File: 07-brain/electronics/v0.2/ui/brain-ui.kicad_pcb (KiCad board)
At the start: 2 copper layers, 58 x 110 mm, 55 parts, among them J1 Conn_02x03_Odd_Even, J2 Conn_01x02, J3 Conn_01x02, J4 Conn_02x02_Odd_Even, J5 Conn_02x03_Odd_Even, J6 Conn_02x02_Odd_Even, J7 Conn_02x05_Odd_Even, J8 Conn_02x03_Odd_Even, Q1 2N3904, Q2 2N3904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

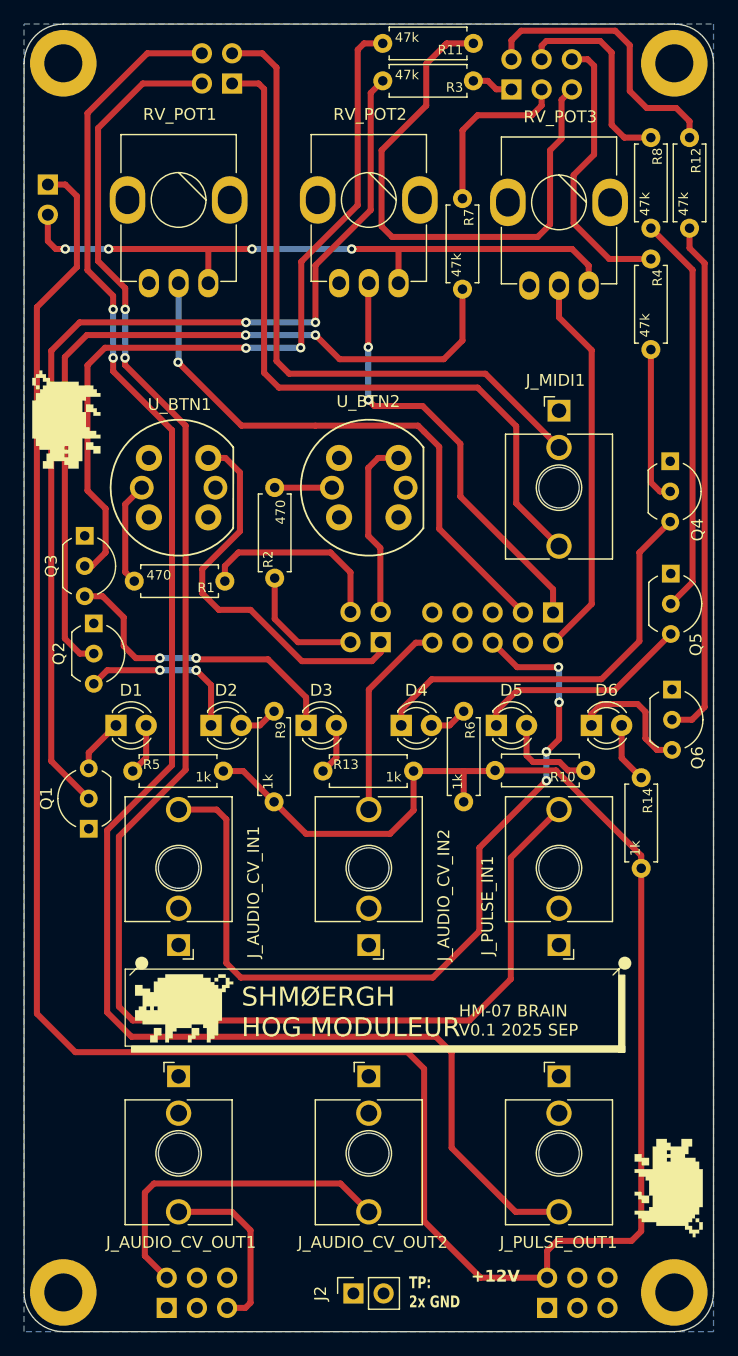
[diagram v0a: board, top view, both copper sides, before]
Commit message: Removed one pot and added one button in Brain
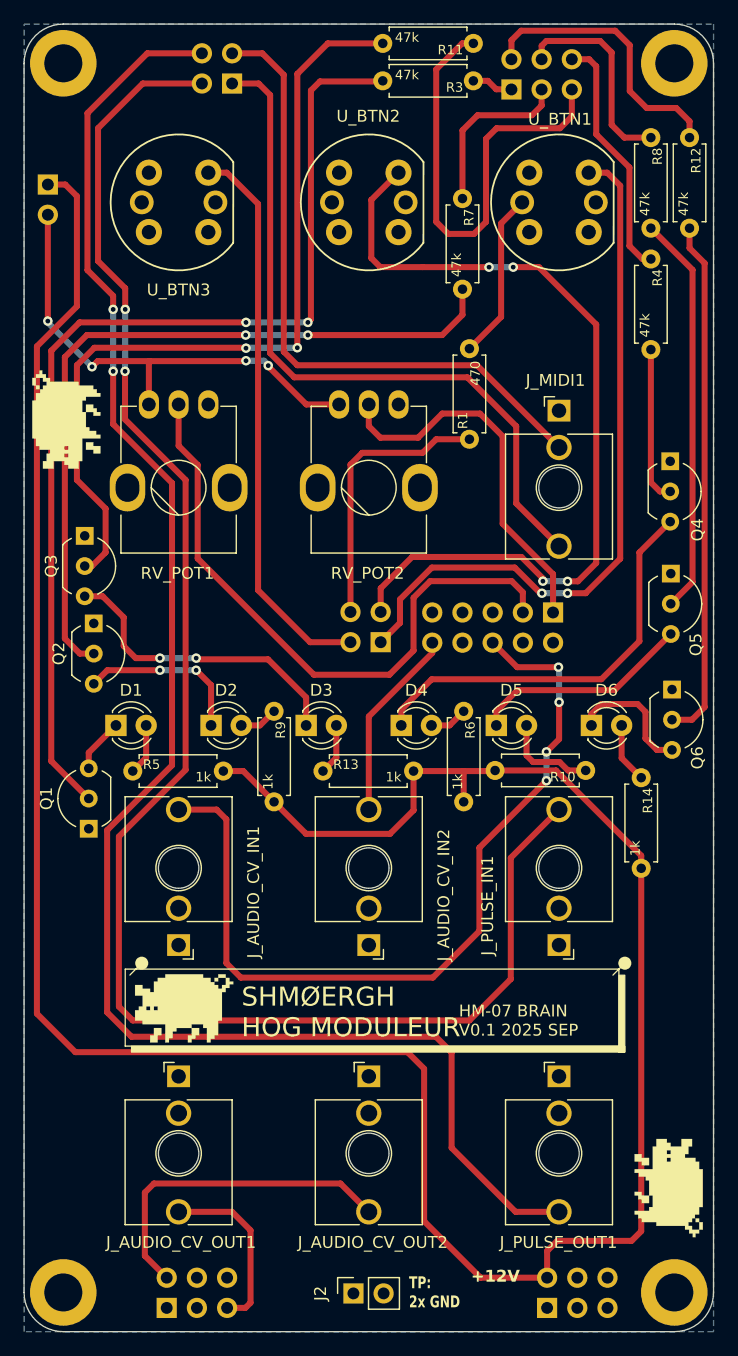
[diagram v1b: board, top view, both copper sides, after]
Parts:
- removed R2: 470, Shmoergh_Custom_Footprints:R_Axial_DIN0207_L6.3mm_D2.5mm_P7.62mm_Horizontal
- removed RV_POT3: 100k, Shmoergh_Custom_Footprints:Potentiometer_Bourns_Single-PTV09A
- added U_BTN3: SW_SPST_Push_LED, Shmoergh_Custom_Footprints:SPST_Circular_Pushbutton_LED, F.Cu at (137.0, 59.0)
- moved U_BTN1 40.0 mm to (169.0, 59.0)
- moved RV_POT1 24.2 mm to (137.0, 83.0), turned to 180 degrees
- moved RV_POT2 24.2 mm to (153.0, 83.0), turned to 180 degrees
- moved U_BTN2 24.0 mm to (153.0, 59.0)
- moved R1 23.8 mm to (161.5, 78.9), turned to 90 degrees
- moved G*** 8.84 mm to (169.0, 69.4)
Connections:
- J4 pad 2: BTN_LED_2 -> BTN_3
- J7 pad 2: POT_3 -> unconnected-(J7-Pin_2-Pad2)
- J7 pad 4: GND -> unconnected-(J7-Pin_4-Pad4)
- J7 pad 5: GND -> unconnected-(J7-Pin_5-Pad5)
- J7 pad 7: GND -> unconnected-(J7-Pin_7-Pad7)
- J7 pad 8: GND -> unconnected-(J7-Pin_8-Pad8)
- J7 pad 9: GND -> unconnected-(J7-Pin_9-Pad9)
- U_BTN2 pad L1: Net-(R2-Pad2) -> unconnected-(U_BTN2-PadL1)
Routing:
- net BTN_2: track 15.4 -> 72.3 mm, vias 0 -> 4
- net BTN_3: track 0.00 -> 47.4 mm
- net POT_3: track 32.5 -> 0.00 mm
- net BTN_1: track 33.2 -> 60.5 mm, vias 0 -> 2
- net +3.3V: track 56.0 -> 40.6 mm
- net BTN_LED_2: track 10.6 -> 0.00 mm
- net LED_3: track 47.1 -> 39.1 mm
- net BTN_LED_1: track 16.3 -> 23.3 mm
- net Net-(R1-Pad2): track 8.75 -> 14.1 mm
- net POT_2: track 36.5 -> 31.7 mm, vias 2 -> 0
- net Net-(R2-Pad2): track 4.82 -> 0.00 mm
- net POT_1: track 48.4 -> 53.0 mm, vias 1 -> 0
- net LED_4: track 23.8 -> 20.8 mm
- net Net-(Q2-B): track 66.7 -> 63.7 mm
- net Net-(Q3-B): track 66.6 -> 69.4 mm
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
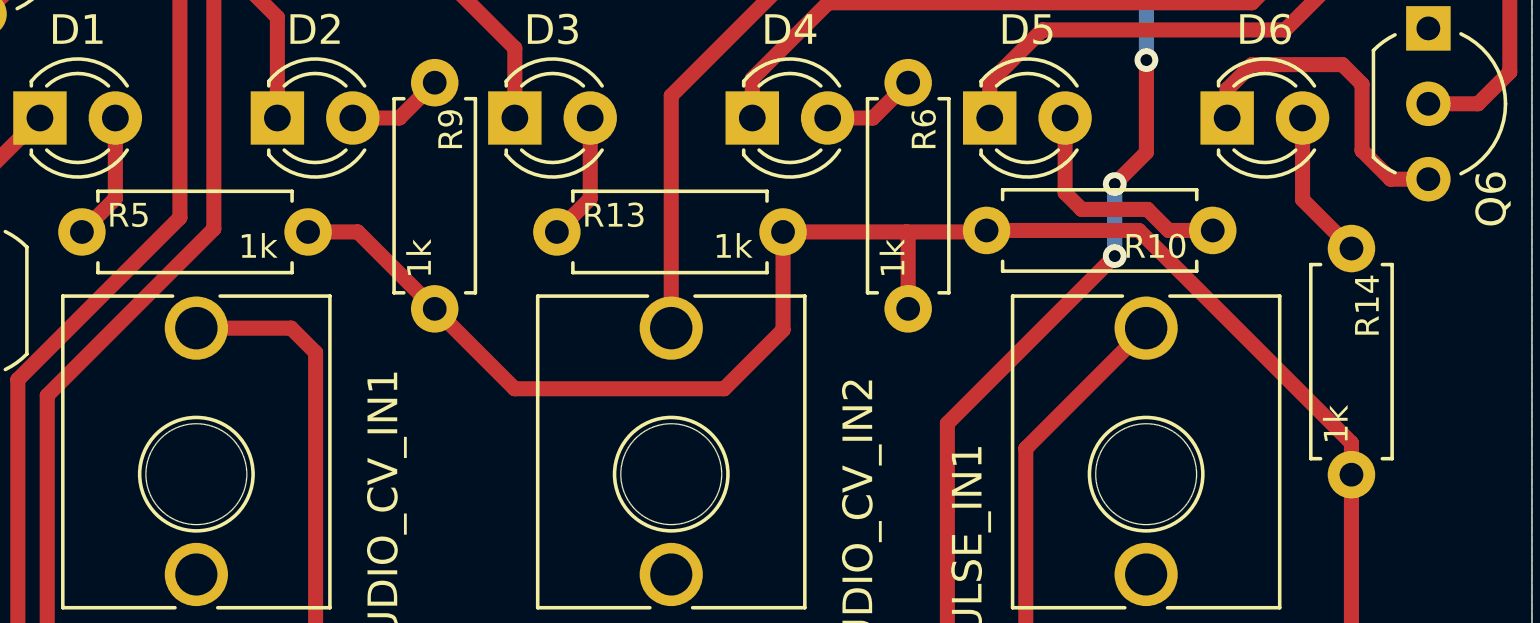
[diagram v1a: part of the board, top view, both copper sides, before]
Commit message: Updated pull-up for MIDI opto in v0.2 Brain
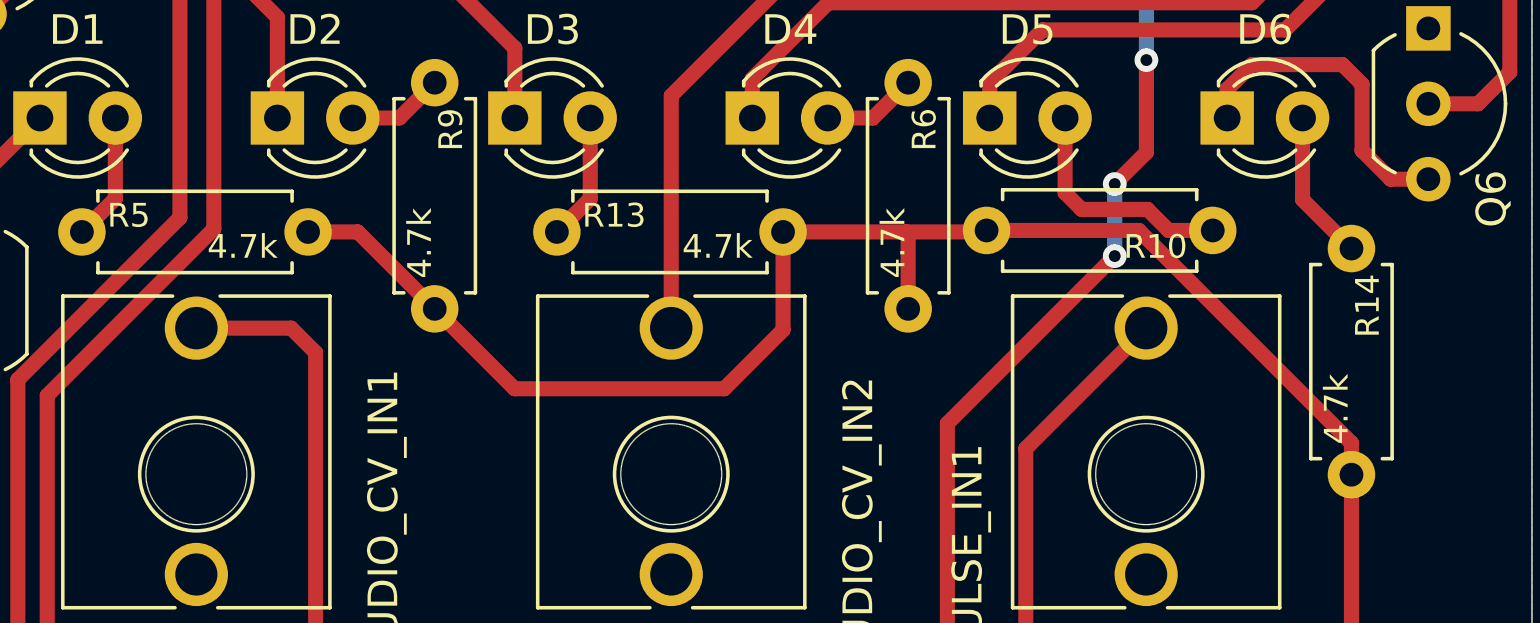
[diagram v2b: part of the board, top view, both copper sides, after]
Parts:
- R10, R13, R14, R5, R6, R9: value 1k -> 4.7k
- U_BTN2, U_BTN3: value SW_SPST_Push_LED -> SW_SPST_Push
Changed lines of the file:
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@@
 			)
 		)
-		(property "Value" "1k"
+		(property "Value" "4.7k"
 			(at 6.6 0.5 90)
 			(layer "F.SilkS")
@@
 			)
 		)
-		(property "Value" "1k"
+		(property "Value" "4.7k"
 			(at 6.6 0.5 0)
 			(layer "F.SilkS")
@@
 			)
 		)
-		(property "Value" "1k"
+		(property "Value" "4.7k"
 			(at 6.6 0.5 90)
 			(layer "F.SilkS")
@@
 			)
 		)
-		(property "Value" "1k"
+		(property "Value" "4.7k"
 			(at 6.6 0.5 0)
 			(layer "F.SilkS")
@@
 			)
 		)
-		(property "Value" "1k"
+		(property "Value" "4.7k"
 			(at 6.6 0.5 0)
 			(layer "F.SilkS")
@@
 			)
 		)
-		(property "Value" "1k"
+		(property "Value" "4.7k"
 			(at 6.6 0.5 90)
 			(layer "F.SilkS")
@@
 			)
 		)
-		(property "Value" "SW_SPST_Push_LED"
+		(property "Value" "SW_SPST_Push"
 			(at 0 -7.366 0)
 			(layer "F.Fab")
@@
 			)
 		)
-		(property "Value" "SW_SPST_Push_LED"
+		(property "Value" "SW_SPST_Push"
 			(at 0 -7.366 0)
 			(layer "F.Fab")
